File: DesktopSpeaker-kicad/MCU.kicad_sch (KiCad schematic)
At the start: 6 parts, among them J6 SWD, U3 STM32G031K8T6

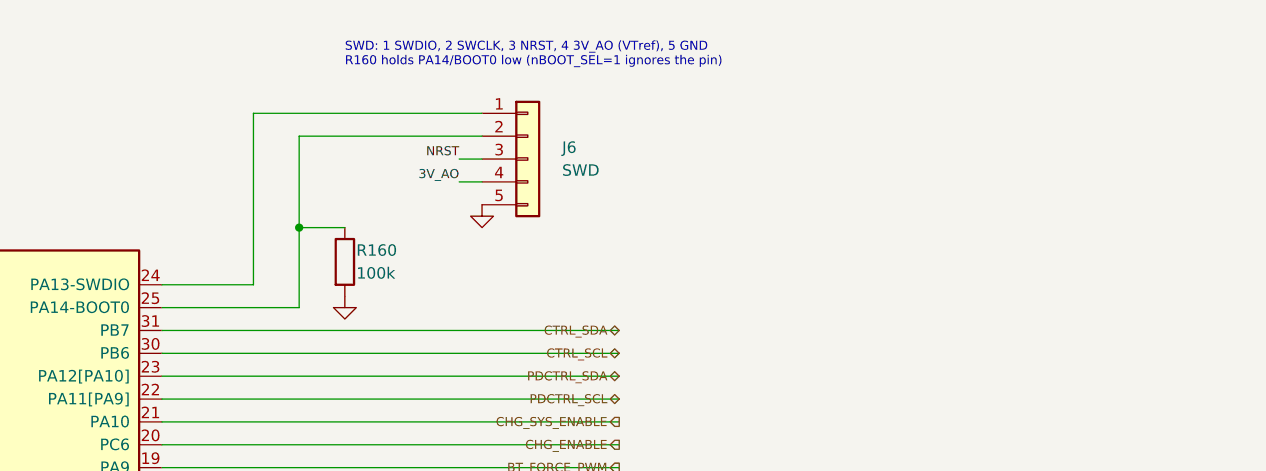
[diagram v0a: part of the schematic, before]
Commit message: Replace SWD header with TC2030-IDC and 4-pin header; set USB audio crystal caps and resistor parts
Co-Authored-By: Claude Sonnet 5.5 <noreply@anthropic.com>
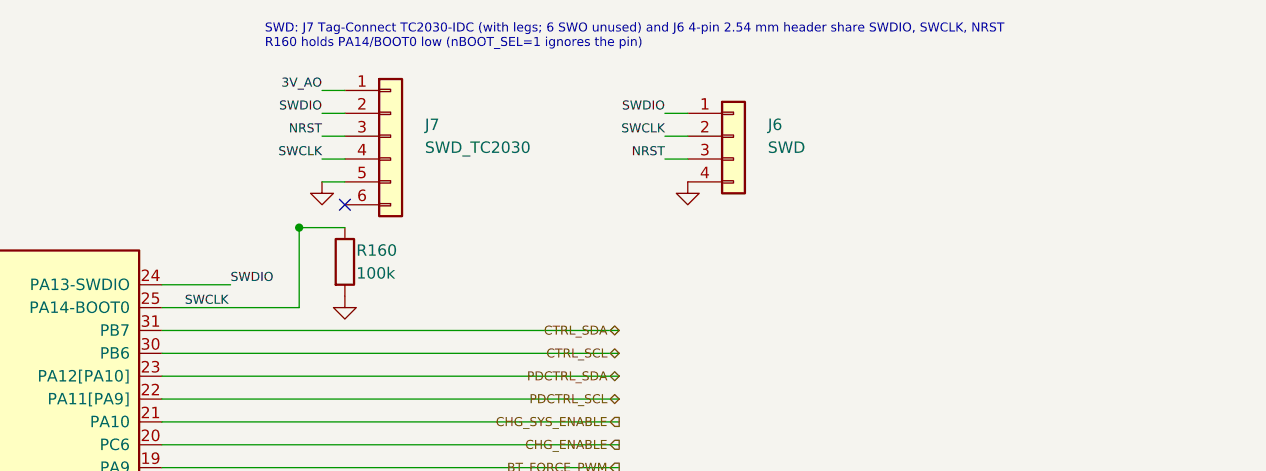
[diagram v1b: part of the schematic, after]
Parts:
- removed J6: SWD, DesktopSpeaker:PinHeader_1x05_P2.54mm_Vertical, symbol Connector_Generic:Conn_01x05
- added J6: SWD, DesktopSpeaker:PinHeader_1x04_P2.54mm_Vertical, symbol Connector_Generic:Conn_01x04
- added J7: SWD_TC2030, DesktopSpeaker:Tag-Connect_TC2030-IDC-FP_2x03_P1.27mm_Vertical, symbol Connector_Generic:Conn_01x06
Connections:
- net 3V_AO: now also J7.1 (Pin_1)
- net GND: now also J6.4 (Pin_4), J7.5 (Pin_5)
- net NRST: now also J6.3 (Pin_3), J7.3 (Pin_3)
- net SWCLK: now reaches R160.1, U3.25 (PA14-BOOT0)
- net SWCLK: now also J6.2 (Pin_2), J7.4 (Pin_4)
- net SWDIO: now reaches U3.24 (PA13-SWDIO)
- net SWDIO: now also J6.1 (Pin_1), J7.2 (Pin_2)
- no-connect marks 14 -> 15
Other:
- note added: "SWD: J7 Tag-Connect TC2030-IDC (with legs; 6 SWO unused) and J6 4-pin 2.54 mm header share SWDIO, SWCLK, NRST R160 holds PA14/BOOT0 low (nBOOT_SEL=1 ignores the pin)"
- note removed: "SWD: 1 SWDIO, 2 SWCLK, 3 NRST, 4 3V_AO (VTref), 5 GND R160 holds PA14/BOOT0 low (nBOOT_SEL=1 ignores the pin)"
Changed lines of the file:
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@@
 (wire (pts (xy 133.35 124.46) (xy 127 124.46)) (stroke (width 0) (type default)))
 (symbol (lib_id "power:GND") (at 127 124.46 0) (unit 1) (exclude_from_sim no) (in_bom no) (on_board no) (dnp no) (property "Reference" "#PWR604" (at 127 128.27 0) (effects (font (size 1.27 1.27)) (hide yes))) (property "Value" "GND" (at 127 129.54 0) (effects (font (size 1.27 1.27)) (hide yes))) (pin "1") (instances (project "DesktopSpeaker" (path "/feda53ed-537d-4f88-9436-c6075776255b/4ab2b160-efba-45d8-be2c-c7b2862cfacf" (reference "#PWR604") (unit 1)))))
-(wire (pts (xy 165.1 82.55) (xy 175.26 82.55)) (stroke (width 0) (type default)))
-(wire (pts (xy 175.26 82.55) (xy 175.26 63.5)) (stroke (width 0) (type default)))
-(wire (pts (xy 175.26 63.5) (xy 200.66 63.5)) (stroke (width 0) (type default)))
+(wire (pts (xy 165.1 82.55) (xy 172.72 82.55)) (stroke (width 0) (type default)))
 (wire (pts (xy 165.1 85.09) (xy 180.34 85.09)) (stroke (width 0) (type default)))
-(wire (pts (xy 180.34 85.09) (xy 180.34 66.04)) (stroke (width 0) (type default)))
-(wire (pts (xy 180.34 66.04) (xy 200.66 66.04)) (stroke (width 0) (type default)))
+(wire (pts (xy 180.34 85.09) (xy 180.34 76.2)) (stroke (width 0) (type default)))
 (wire (pts (xy 180.34 76.2) (xy 185.42 76.2)) (stroke (width 0) (type default)))
 (junction (at 180.34 76.2) (diameter 0) (color 0 0 0 0))
 (symbol (lib_id "PD_R:PD_R") (at 185.42 80.01 0) (unit 1) (exclude_from_sim no) (in_bom yes) (on_board yes) (dnp no) (property "Reference" "R160" (at 186.69 78.74 0) (effects (font (size 1.27 1.27)) (justify left))) (property "Value" "100k" (at 186.69 81.28 0) (effects (font (size 1.27 1.27)) (justify left))) (property "Footprint" "DesktopSpeaker:PD_R_0603" (at 185.42 80.01 0) (hide yes) (effects (font (size 1.27 1.27)))) (property "MPN" "RC0603FR-07100KL" (at 185.42 80.01 0) (hide yes) (effects (font (size 1.27 1.27)))) (property "Manufacturer" "YAGEO" (at 185.42 80.01 0) (hide yes) (effects (font (size 1 1)))) (property "LCSC" "C14675" (at 185.42 80.01 0) (hide yes) (effects (font (size 1 1)))) (property "Datasheet" "${KIPRJMOD}/../ai-files/datasheets/Yageo_RC0603FR_series.pdf" (at 185.42 80.01 0) (hide yes) (effects (font (size 1 1)))) (pin "1") (pin "2") (instances (project "DesktopSpeaker" (path "/feda53ed-537d-4f88-9436-c6075776255b/4ab2b160-efba-45d8-be2c-c7b2862cfacf" (reference "R160") (unit 1)))))
 (symbol (lib_id "power:GND") (at 185.42 83.82 0) (unit 1) (exclude_from_sim no) (in_bom no) (on_board no) (dnp no) (property "Reference" "#PWR605" (at 185.42 87.63 0) (effects (font (size 1.27 1.27)) (hide yes))) (property "Value" "GND" (at 185.42 88.9 0) (effects (font (size 1.27 1.27)) (hide yes))) (pin "1") (instances (project "DesktopSpeaker" (path "/feda53ed-537d-4f88-9436-c6075776255b/4ab2b160-efba-45d8-be2c-c7b2862cfacf" (reference "#PWR605") (unit 1)))))
-(wire (pts (xy 200.66 68.58) (xy 198.12 68.58)) (stroke (width 0) (type default)))
-(label "NRST" (at 198.12 68.58 0) (effects (font (size 1 1)) (justify right bottom)))
-(wire (pts (xy 200.66 71.12) (xy 198.12 71.12)) (stroke (width 0) (type default)))
-(label "3V_AO" (at 198.12 71.12 0) (effects (font (size 1 1)) (justify right bottom)))
-(symbol (lib_id "power:GND") (at 200.66 73.66 0) (unit 1) (exclude_from_sim no) (in_bom no) (on_board no) (dnp no) (property "Reference" "#PWR606" (at 200.66 77.47 0) (effects (font (size 1.27 1.27)) (hide yes))) (property "Value" "GND" (at 200.66 78.74 0) (effects (font (size 1.27 1.27)) (hide yes))) (pin "1") (instances (project "DesktopSpeaker" (path "/feda53ed-537d-4f88-9436-c6075776255b/4ab2b160-efba-45d8-be2c-c7b2862cfacf" (reference "#PWR606") (unit 1)))))
-(symbol (lib_id "Connector_Generic:Conn_01x05") (at 205.74 68.58 0) (unit 1) (exclude_from_sim no) (in_bom yes) (on_board yes) (dnp no) (property "Reference" "J6" (at 209.55 67.31 0) (effects (font (size 1.27 1.27)) (justify left))) (property "Value" "SWD" (at 209.55 69.85 0) (effects (font (size 1.27 1.27)) (justify left))) (property "Footprint" "DesktopSpeaker:PinHeader_1x05_P2.54mm_Vertical" (at 205.74 68.58 0) (hide yes) (effects (font (size 1 1)))) (property "Manufacturer" "XYECONN" (at 205.74 68.58 0) (hide yes) (effects (font (size 1 1)))) (property "MPN" "XY-MTP254-1X5" (at 205.74 68.58 0) (hide yes) (effects (font (size 1 1)))) (property "LCSC" "C54110162" (at 205.74 68.58 0) (hide yes) (effects (font (size 1 1)))) (pin "1") (pin "2") (pin "3") (pin "4") (pin "5") (instances (project "DesktopSpeaker" (path "/feda53ed-537d-4f88-9436-c6075776255b/4ab2b160-efba-45d8-be2c-c7b2862cfacf" (reference "J6") (unit 1)))))
-(text "SWD: 1 SWDIO, 2 SWCLK, 3 NRST, 4 3V_AO (VTref), 5 GND\nR160 holds PA14/BOOT0 low (nBOOT_SEL=1 ignores the pin)" (at 185.42 58.42 0) (effects (font (size 1 1)) (justify left bottom)))
 (wire (pts (xy 165.1 87.63) (xy 215.9 87.63)) (stroke (width 0) (type default)))
 (hierarchical_label "CTRL_SDA" (shape bidirectional) (at 215.9 87.63 0) (effects (font (size 1.0 1.0)) (justify right bottom)))
@@
 (text "Reserved (no-connect): see ai-files/reports/mcu-pin-allocation.md" (at 45.72 140.97 0) (effects (font (size 1 1)) (justify left bottom)))
 (text "3V_AO supply: 100nF + 4.7uF at VDD/VDDA (DS12992 fig. 13); NRST 100nF, internal pull-up" (at 45.72 60.96 0) (effects (font (size 1 1)) (justify left bottom)))
+(label "SWDIO" (at 172.72 82.55 0) (effects (font (size 1 1)) (justify left bottom)))
+(label "SWCLK" (at 167.64 85.09 0) (effects (font (size 1 1)) (justify left bottom)))
+(wire (pts (xy 185.42 60.96) (xy 182.88 60.96)) (stroke (width 0) (type default)))
+(label "3V_AO" (at 182.88 60.96 0) (effects (font (size 1 1)) (justify right bottom)))
+(wire (pts (xy 185.42 63.5) (xy 182.88 63.5)) (stroke (width 0) (type default)))
+(label "SWDIO" (at 182.88 63.5 0) (effects (font (size 1 1)) (justify right bottom)))
+(wire (pts (xy 185.42 66.04) (xy 182.88 66.04)) (stroke (width 0) (type default)))
+(label "NRST" (at 182.88 66.04 0) (effects (font (size 1 1)) (justify right bottom)))
+(wire (pts (xy 185.42 68.58) (xy 182.88 68.58)) (stroke (width 0) (type default)))
+(label "SWCLK" (at 182.88 68.58 0) (effects (font (size 1 1)) (justify right bottom)))
+(wire (pts (xy 185.42 71.12) (xy 182.88 71.12)) (stroke (width 0) (type default)))
+(symbol (lib_id "power:GND") (at 182.88 71.12 0) (unit 1) (exclude_from_sim no) (in_bom no) (on_board no) (dnp no) (property "Reference" "#PWR610" (at 182.88 74.93 0) (effects (font (size 1.27 1.27)) (hide yes))) (property "Value" "GND" (at 182.88 76.2 0) (effects (font (size 1.27 1.27)) (hide yes))) (pin "1") (instances (project "DesktopSpeaker" (path "/feda53ed-537d-4f88-9436-c6075776255b/4ab2b160-efba-45d8-be2c-c7b2862cfacf" (reference "#PWR610") (unit 1)))))
+(no_connect (at 185.42 73.66))
+(symbol (lib_id "Connector_Generic:Conn_01x06") (at 190.5 66.04 0) (unit 1) (exclude_from_sim no) (in_bom no) (on_board yes) (dnp no) (property "Reference" "J7" (at 194.31 64.77 0) (effects (font (size 1.27 1.27)) (justify left))) (property "Value" "SWD_TC2030" (at 194.31 67.31 0) (effects (font (size 1.27 1.27)) (justify left))) (property "Footprint" "DesktopSpeaker:Tag-Connect_TC2030-IDC-FP_2x03_P1.27mm_Vertical" (at 190.5 66.04 0) (hide yes) (effects (font (size 1 1)))) (property "Manufacturer" "Tag-Connect" (at 190.5 66.04 0) (hide yes) (effects (font (size 1 1)))) (property "MPN" "TC2030-IDC" (at 190.5 66.04 0) (hide yes) (effects (font (size 1 1)))) (property "LCSC" "" (at 190.5 66.04 0) (hide yes) (effects (font (size 1 1)))) (pin "1") (pin "2") (pin "3") (pin "4") (pin "5") (pin "6") (instances (project "DesktopSpeaker" (path "/feda53ed-537d-4f88-9436-c6075776255b/4ab2b160-efba-45d8-be2c-c7b2862cfacf" (reference "J7") (unit 1)))))
+(wire (pts (xy 223.52 63.5) (xy 220.98 63.5)) (stroke (width 0) (type default)))
+(label "SWDIO" (at 220.98 63.5 0) (effects (font (size 1 1)) (justify right bottom)))
+(wire (pts (xy 223.52 66.04) (xy 220.98 66.04)) (stroke (width 0) (type default)))
+(label "SWCLK" (at 220.98 66.04 0) (effects (font (size 1 1)) (justify right bottom)))
+(wire (pts (xy 223.52 68.58) (xy 220.98 68.58)) (stroke (width 0) (type default)))
+(label "NRST" (at 220.98 68.58 0) (effects (font (size 1 1)) (justify right bottom)))
+(symbol (lib_id "power:GND") (at 223.52 71.12 0) (unit 1) (exclude_from_sim no) (in_bom no) (on_board no) (dnp no) (property "Reference" "#PWR611" (at 223.52 74.93 0) (effects (font (size 1.27 1.27)) (hide yes))) (property "Value" "GND" (at 223.52 76.2 0) (effects (font (size 1.27 1.27)) (hide yes))) (pin "1") (instances (project "DesktopSpeaker" (path "/feda53ed-537d-4f88-9436-c6075776255b/4ab2b160-efba-45d8-be2c-c7b2862cfacf" (reference "#PWR611") (unit 1)))))
+(symbol (lib_id "Connector_Generic:Conn_01x04") (at 228.6 66.04 0) (unit 1) (exclude_from_sim no) (in_bom yes) (on_board yes) (dnp no) (property "Reference" "J6" (at 232.41 64.77 0) (effects (font (size 1.27 1.27)) (justify left))) (property "Value" "SWD" (at 232.41 67.31 0) (effects (font (size 1.27 1.27)) (justify left))) (property "Footprint" "DesktopSpeaker:PinHeader_1x04_P2.54mm_Vertical" (at 228.6 66.04 0) (hide yes) (effects (font (size 1 1)))) (property "Manufacturer" "Ckmtw" (at 228.6 66.04 0) (hide yes) (effects (font (size 1 1)))) (property "MPN" "B-2100S04P-A110" (at 228.6 66.04 0) (hide yes) (effects (font (size 1 1)))) (property "LCSC" "C124378" (at 228.6 66.04 0) (hide yes) (effects (font (size 1 1)))) (pin "1") (pin "2") (pin "3") (pin "4") (instances (project "DesktopSpeaker" (path "/feda53ed-537d-4f88-9436-c6075776255b/4ab2b160-efba-45d8-be2c-c7b2862cfacf" (reference "J6") (unit 1)))))
+(text "SWD: J7 Tag-Connect TC2030-IDC (with legs; 6 SWO unused) and J6 4-pin 2.54 mm header share SWDIO, SWCLK, NRST\nR160 holds PA14/BOOT0 low (nBOOT_SEL=1 ignores the pin)" (at 176.53 56.39 0) (effects (font (size 1 1)) (justify left bottom)))
 )

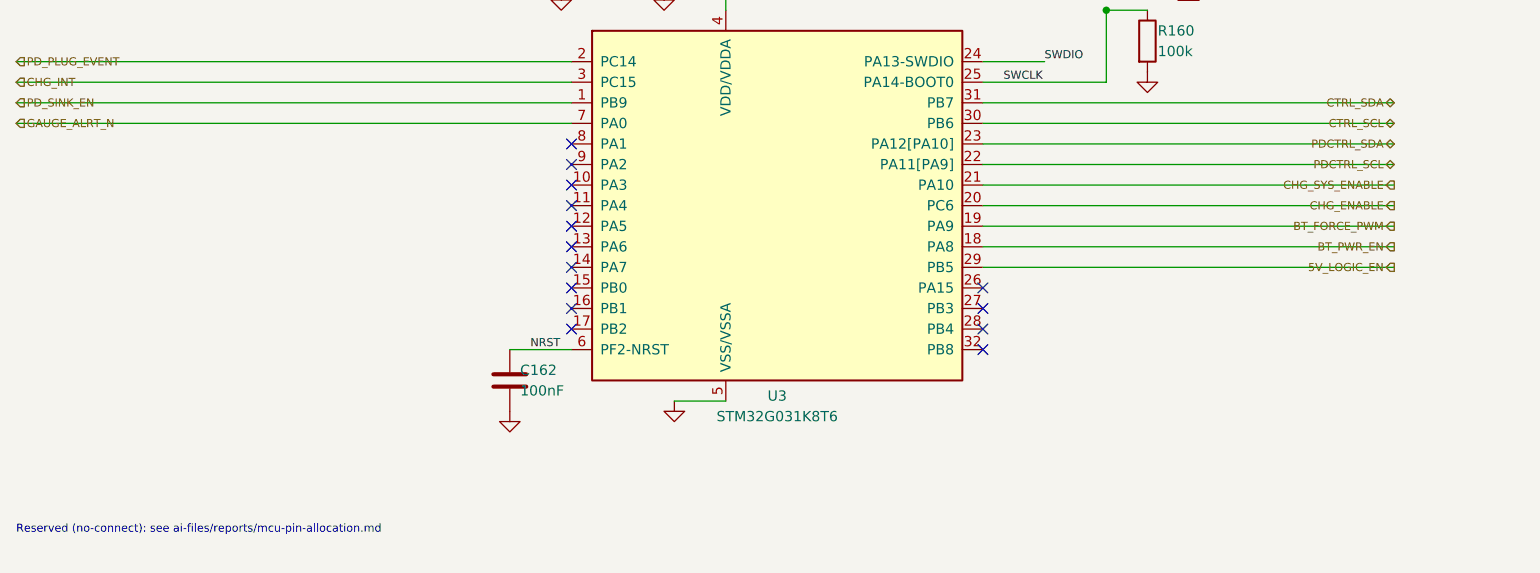
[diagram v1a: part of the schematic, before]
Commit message: Capture Bluetooth BM83 child sheet with MCU UART/reset/MFB connections
Co-Authored-By: Claude Sonnet 5.5 <noreply@anthropic.com>
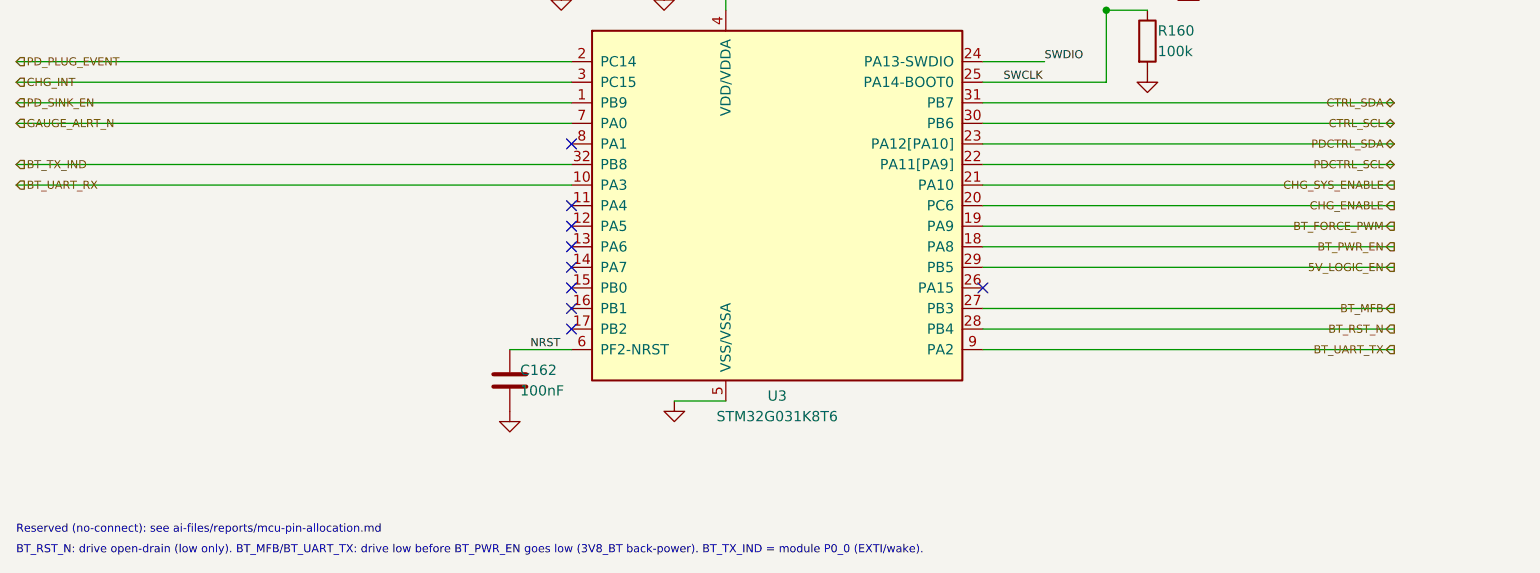
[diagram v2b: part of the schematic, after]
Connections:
- net BT_UART_RX: now reaches U3.10 (PA3)
- net BT_MFB: now reaches U3.27 (PB3)
- net BT_RST_N: now reaches U3.28 (PB4)
- net BT_TX_IND: now reaches U3.32 (PB8)
- net BT_UART_TX: now reaches U3.9 (PA2)
- no-connect marks 15 -> 10
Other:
- note added: "BT_RST_N: drive open-drain (low only). BT_MFB/BT_UART_TX: drive low before BT_PWR_EN goes low (3V8_BT back-power). BT_TX_IND = module P0_0 (EXTI/wake)."
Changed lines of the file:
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@@
 (hierarchical_label "GAUGE_ALRT_N" (shape input) (at 45.72 90.17 0) (effects (font (size 1.0 1.0)) (justify left bottom)))
 (no_connect (at 114.3 92.71))
-(no_connect (at 114.3 95.25))
-(no_connect (at 114.3 97.79))
 (no_connect (at 114.3 100.33))
 (no_connect (at 114.3 102.87))
@@
 (hierarchical_label "5V_LOGIC_EN" (shape output) (at 215.9 107.95 0) (effects (font (size 1.0 1.0)) (justify right bottom)))
 (no_connect (at 165.1 110.49))
-(no_connect (at 165.1 113.03))
-(no_connect (at 165.1 115.57))
-(no_connect (at 165.1 118.11))
 (text "Reserved (no-connect): see ai-files/reports/mcu-pin-allocation.md" (at 45.72 140.97 0) (effects (font (size 1 1)) (justify left bottom)))
 (text "3V_AO supply: 100nF + 4.7uF at VDD/VDDA (DS12992 fig. 13); NRST 100nF, internal pull-up" (at 45.72 60.96 0) (effects (font (size 1 1)) (justify left bottom)))
@@
 (symbol (lib_id "Connector_Generic:Conn_01x04") (at 228.6 66.04 0) (unit 1) (exclude_from_sim no) (in_bom yes) (on_board yes) (dnp no) (property "Reference" "J6" (at 232.41 64.77 0) (effects (font (size 1.27 1.27)) (justify left))) (property "Value" "SWD" (at 232.41 67.31 0) (effects (font (size 1.27 1.27)) (justify left))) (property "Footprint" "DesktopSpeaker:PinHeader_1x04_P2.54mm_Vertical" (at 228.6 66.04 0) (hide yes) (effects (font (size 1 1)))) (property "Manufacturer" "Ckmtw" (at 228.6 66.04 0) (hide yes) (effects (font (size 1 1)))) (property "MPN" "B-2100S04P-A110" (at 228.6 66.04 0) (hide yes) (effects (font (size 1 1)))) (property "LCSC" "C124378" (at 228.6 66.04 0) (hide yes) (effects (font (size 1 1)))) (pin "1") (pin "2") (pin "3") (pin "4") (instances (project "DesktopSpeaker" (path "/feda53ed-537d-4f88-9436-c6075776255b/4ab2b160-efba-45d8-be2c-c7b2862cfacf" (reference "J6") (unit 1)))))
 (text "SWD: J7 Tag-Connect TC2030-IDC (with legs; 6 SWO unused) and J6 4-pin 2.54 mm header share SWDIO, SWCLK, NRST\nR160 holds PA14/BOOT0 low (nBOOT_SEL=1 ignores the pin)" (at 176.53 56.39 0) (effects (font (size 1 1)) (justify left bottom)))
+(wire (pts (xy 45.72 95.25) (xy 114.3 95.25)) (stroke (width 0) (type default)))
+(hierarchical_label "BT_TX_IND" (shape input) (at 45.72 95.25 0) (effects (font (size 1.0 1.0)) (justify left bottom)))
+(wire (pts (xy 45.72 97.79) (xy 114.3 97.79)) (stroke (width 0) (type default)))
+(hierarchical_label "BT_UART_RX" (shape input) (at 45.72 97.79 0) (effects (font (size 1.0 1.0)) (justify left bottom)))
+(wire (pts (xy 165.1 113.03) (xy 215.9 113.03)) (stroke (width 0) (type default)))
+(hierarchical_label "BT_MFB" (shape output) (at 215.9 113.03 0) (effects (font (size 1.0 1.0)) (justify right bottom)))
+(wire (pts (xy 165.1 115.57) (xy 215.9 115.57)) (stroke (width 0) (type default)))
+(hierarchical_label "BT_RST_N" (shape output) (at 215.9 115.57 0) (effects (font (size 1.0 1.0)) (justify right bottom)))
+(wire (pts (xy 165.1 118.11) (xy 215.9 118.11)) (stroke (width 0) (type default)))
+(hierarchical_label "BT_UART_TX" (shape output) (at 215.9 118.11 0) (effects (font (size 1.0 1.0)) (justify right bottom)))
+(text "BT_RST_N: drive open-drain (low only). BT_MFB/BT_UART_TX: drive low before BT_PWR_EN goes low (3V8_BT back-power). BT_TX_IND = module P0_0 (EXTI/wake)." (at 45.72 143.51 0) (effects (font (size 1 1)) (justify left bottom)))
 )
